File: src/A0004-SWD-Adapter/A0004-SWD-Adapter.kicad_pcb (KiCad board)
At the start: 2 copper layers, 40.6 x 50.3 mm, 13 parts, among them P1 LARGE_SBH11-PBPC-D10-RA-BK_1, P2 SMALL_3220-20-0200-00

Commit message: routed board with new programmer connectors
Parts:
- removed LOGO1: Logo, A0004-SWD-Adapter:Logo
- added P3: 0530470610, Full-Flight-Computer:53047-0610, F.Cu at (135.3, 122.7)
- added P4: 0530470610, Full-Flight-Computer:53047-0610, F.Cu at (135.6, 79.4)
- TP3: moved to B.Cu
- turned TP3 to 180 degrees
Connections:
- net /MCU_VDD1 renamed MCU_VDD
- net /NRST renamed NRST
- net /SWCLK renamed SWCLK
- net /SWDIO renamed SWDIO
- net /SWO renamed SWO
- P1 pad 10: /GND10 -> Earth
- P1 pad 11: /NC_11 -> unconnected-(P1-Pad11)
- P1 pad 12: /GND12 -> Earth
- P1 pad 14: /GND14 -> Earth
- P1 pad 16: /GND16 -> Earth
- P1 pad 17: /NC_17 -> unconnected-(P1-Pad17)
- P1 pad 18: /GND18 -> Earth
- P1 pad 19: /NC_19 -> unconnected-(P1-Pad19)
- P1 pad 2: /NC_2 -> unconnected-(P1-Pad2)
- P1 pad 20: /GND20 -> Earth
- P1 pad 3: /NC_3 -> unconnected-(P1-Pad3)
- P1 pad 4: /GND4 -> Earth
- P1 pad 5: /NC_5 -> unconnected-(P1-Pad5)
- P1 pad 6: /GND6 -> Earth
- P1 pad 8: /GND8 -> unconnected-(P1-Pad8)
- P2 pad 10: /GND10 -> Earth
- P2 pad 11: /NC_11 -> unconnected-(P2-Pad11)
- P2 pad 12: /GND12 -> Earth
- P2 pad 14: /GND14 -> Earth
- P2 pad 16: /GND16 -> Earth
- P2 pad 17: /NC_17 -> unconnected-(P2-Pad17)
- P2 pad 18: /GND18 -> Earth
- P2 pad 19: /NC_19 -> unconnected-(P2-Pad19)
- P2 pad 2: /NC_2 -> unconnected-(P2-Pad2)
- P2 pad 20: /GND20 -> Earth
- P2 pad 3: /NC_3 -> unconnected-(P2-Pad3)
- P2 pad 4: /GND4 -> Earth
- P2 pad 5: /NC_5 -> unconnected-(P2-Pad5)
- P2 pad 6: /GND6 -> Earth
- P2 pad 8: /GND8 -> unconnected-(P2-Pad8)
- TP3 pad 1: /GND4 -> Earth
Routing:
- net /GND14: track 80.6 -> 0.00 mm, vias 2 -> 0
- net /GND18: track 75.1 -> 0.00 mm, vias 2 -> 0
- net /GND4: track 73.6 -> 0.00 mm, vias 1 -> 0
- net /GND16: track 72.8 -> 0.00 mm, vias 2 -> 0
- net /GND8: track 64.7 -> 0.00 mm, vias 1 -> 0
- net /GND10: track 64.3 -> 0.00 mm, vias 2 -> 0
- net /GND12: track 63.9 -> 0.00 mm, vias 1 -> 0
- net /GND6: track 60.8 -> 0.00 mm, vias 2 -> 0
- net /NC_2: track 57.2 -> 0.00 mm, vias 1 -> 0
- net /GND20: track 57.1 -> 0.00 mm, vias 2 -> 0
- net SWCLK: track 30.8 -> 76.0 mm, vias 2 -> 3
- net /NC_19: track 44.9 -> 0.00 mm, vias 2 -> 0
- net SWDIO: track 35.3 -> 75.9 mm, vias 2 -> 3
- net SWO: track 30.9 -> 71.5 mm
- net /NC_3: track 40.1 -> 0.00 mm, vias 2 -> 0
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- added copper zone on B.Cu, net Earth
- added copper zone on F.Cu, net MCU_VDD
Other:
- board text added: "A0005 SWD Adapter Rev 1.0"
- board text added: "Crossover Wiring"
- board text added: "Straight Wiring"
- board text removed: "A0004 SWD Adapter Rev 1.0"

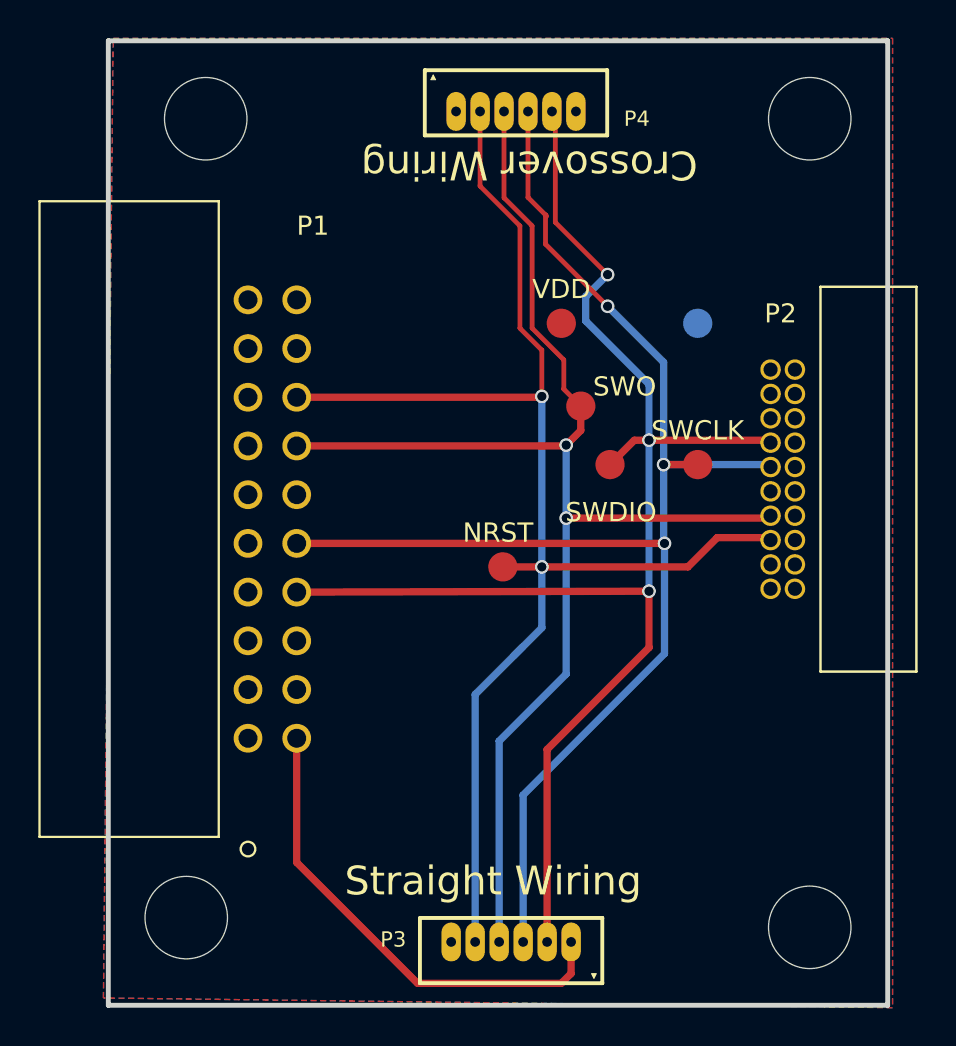
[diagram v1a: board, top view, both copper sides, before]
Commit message: resolved layout DRC errors and generated fabrication outputs
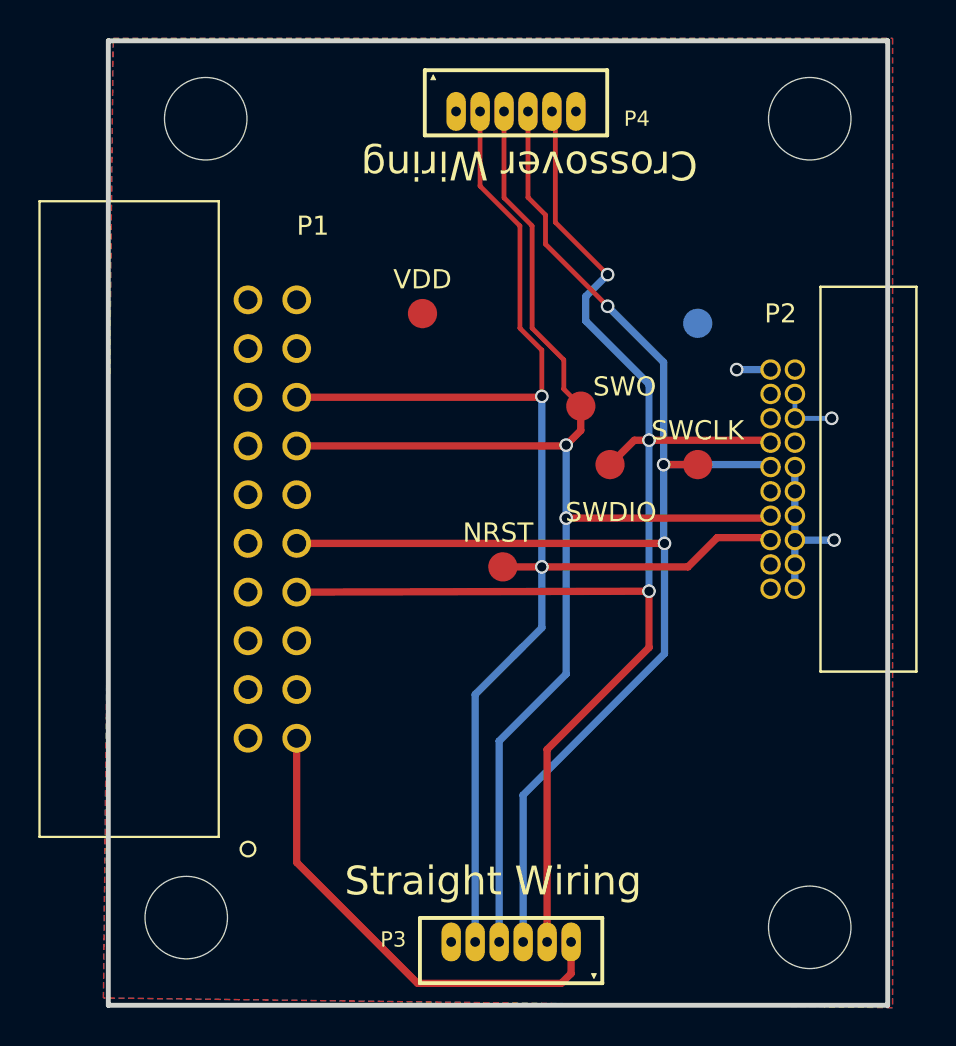
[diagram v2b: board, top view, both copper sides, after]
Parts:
- moved TP1 7.26 mm to (130.7, 89.9)
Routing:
- net Earth: track 0.52 -> 11.6 mm, vias 0 -> 2
- net MCU_VDD: track 25.3 -> 27.0 mm, vias 0 -> 1
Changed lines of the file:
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@@
       (drillshape 0)
       (scaleselection 1)
-      (outputdirectory "../../production/")
+      (outputdirectory "../../production/gerbers/")
     )
   )
@@
   )
   (footprint "A0004-SWD-Adapter:TP" (layer "F.Cu")
-    (at 137.922 90.424)
-    (property "Sheetfile" "A0004-SWD-Adapter.kicad_sch")
-    (property "Sheetname" "")
-    (attr through_hole)
+    (at 130.683 89.916)
+    (property "Sheetfile" "A0004-SWD-Adapter.kicad_sch")
+    (property "Sheetname" "")
+    (attr smd)
     (fp_text reference "TP1" (at 0 -1.9812) (layer "F.SilkS") hide
         (effects (font (size 1 1) (thickness 0.15)))
@@
     (property "Sheetfile" "A0004-SWD-Adapter.kicad_sch")
     (property "Sheetname" "")
-    (attr through_hole)
+    (attr smd)
     (fp_text reference "TP6" (at 0 -1.9812) (layer "F.SilkS") hide
         (effects (font (size 1 1) (thickness 0.15)))
@@
     (property "Sheetfile" "A0004-SWD-Adapter.kicad_sch")
     (property "Sheetname" "")
-    (attr through_hole)
+    (attr smd)
     (fp_text reference "TP4" (at 0 -1.9812) (layer "F.SilkS") hide
         (effects (font (size 1 1) (thickness 0.15)))
@@
     (property "Sheetfile" "A0004-SWD-Adapter.kicad_sch")
     (property "Sheetname" "")
-    (attr through_hole)
+    (attr smd)
     (fp_text reference "TP7" (at 0 -1.9812) (layer "F.SilkS") hide
         (effects (font (size 1 1) (thickness 0.15)))
@@
   (segment (start 138.43 124.333) (end 137.922 124.841) (width 0.381) (layer "F.Cu") (net 1))
   (segment (start 130.429 124.841) (end 124.12345 118.53545) (width 0.381) (layer "F.Cu") (net 1))
-  (segment (start 150.10295 94.107) (end 150.241 94.107) (width 0.25) (layer "F.Cu") (net 4))
-  (segment (start 121.58345 109.52) (end 121.204 109.52) (width 0.381) (layer "F.Cu") (net 4))
+  (via (at 147.066 92.837) (size 0.7112) (drill 0.4826) (layers "F.Cu" "B.Cu") (net 1))
+  (segment (start 148.83295 92.837) (end 147.066 92.837) (width 0.381) (layer "B.Cu") (net 1))
+  (via (at 152.019 95.377) (size 0.7112) (drill 0.4826) (layers "F.Cu" "B.Cu") (net 4))
+  (via (at 152.146 101.727) (size 0.7112) (drill 0.4826) (layers "F.Cu" "B.Cu") (net 4))
+  (segment (start 150.10295 94.107) (end 150.10295 95.377) (width 0.25) (layer "B.Cu") (net 4))
+  (segment (start 150.10295 99.187) (end 150.10295 100.457) (width 0.381) (layer "B.Cu") (net 4))
+  (segment (start 150.10295 97.917) (end 150.10295 99.187) (width 0.381) (layer "B.Cu") (net 4))
+  (segment (start 150.10295 100.457) (end 150.10295 101.727) (width 0.381) (layer "B.Cu") (net 4))
+  (segment (start 150.10295 102.997) (end 150.10295 104.267) (width 0.381) (layer "B.Cu") (net 4))
+  (segment (start 150.10295 101.727) (end 152.146 101.727) (width 0.381) (layer "B.Cu") (net 4))
+  (segment (start 150.10295 95.377) (end 152.019 95.377) (width 0.25) (layer "B.Cu") (net 4))
+  (segment (start 150.10295 101.727) (end 150.10295 102.997) (width 0.381) (layer "B.Cu") (net 4))
   (segment (start 137.61 79.551) (end 137.61 85.159) (width 0.25) (layer "F.Cu") (net 6))
   (segment (start 137.18 122.682) (end 137.18 112.649) (width 0.381) (layer "F.Cu") (net 6))
@@
   (segment (start 142.494 93.599) (end 139.192 90.297) (width 0.381) (layer "B.Cu") (net 6))
   (segment (start 139.192 89.027) (end 140.335 87.884) (width 0.381) (layer "B.Cu") (net 6))
-  (segment (start 121.58345 104.44) (end 121.458 104.44) (width 0.381) (layer "B.Cu") (net 7))
   (segment (start 136.184 79.375) (end 136.184 83.86) (width 0.25) (layer "F.Cu") (net 8))
   (segment (start 124.12345 101.9) (end 143.302 101.9) (width 0.381) (layer "F.Cu") (net 8))
   (segment (start 137.0965 84.7725) (end 137.0965 86.2965) (width 0.25) (layer "F.Cu") (net 8))
   (segment (start 137.0965 86.2965) (end 140.335 89.535) (width 0.25) (layer "F.Cu") (net 8))
-  (segment (start 137.0965 84.7725) (end 137.16 84.836) (width 0.25) (layer "F.Cu") (net 8))
   (segment (start 136.184 83.86) (end 137.0965 84.7725) (width 0.25) (layer "F.Cu") (net 8))
   (segment (start 145.034 97.79) (end 143.256 97.79) (width 0.381) (layer "F.Cu") (net 8))
@@
   (segment (start 136.906 94.234) (end 136.906 103.124) (width 0.381) (layer "B.Cu") (net 11))
   (segment (start 133.43 122.682) (end 133.43 109.775) (width 0.381) (layer "B.Cu") (net 11))
-  (segment (start 148.544 95.204) (end 148.844 95.504) (width 0.381) (layer "F.Cu") (net 16))
   (zone (net 1) (net_name "MCU_VDD") (layer "F.Cu") (hatch edge 0.5)
     (connect_pads (clearance 0.508))
     (min_thickness 0.25) (filled_areas_thickness no)
-    (fill yes (thermal_gap 0.5) (thermal_bridge_width 0.5))
+    (fill yes (thermal_gap 0.381) (thermal_bridge_width 0.381))
     (polygon
       (pts
